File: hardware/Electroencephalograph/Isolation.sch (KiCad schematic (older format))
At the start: 14 parts, among them U4 THI3-0511, U5 ADUM2401BRWZ

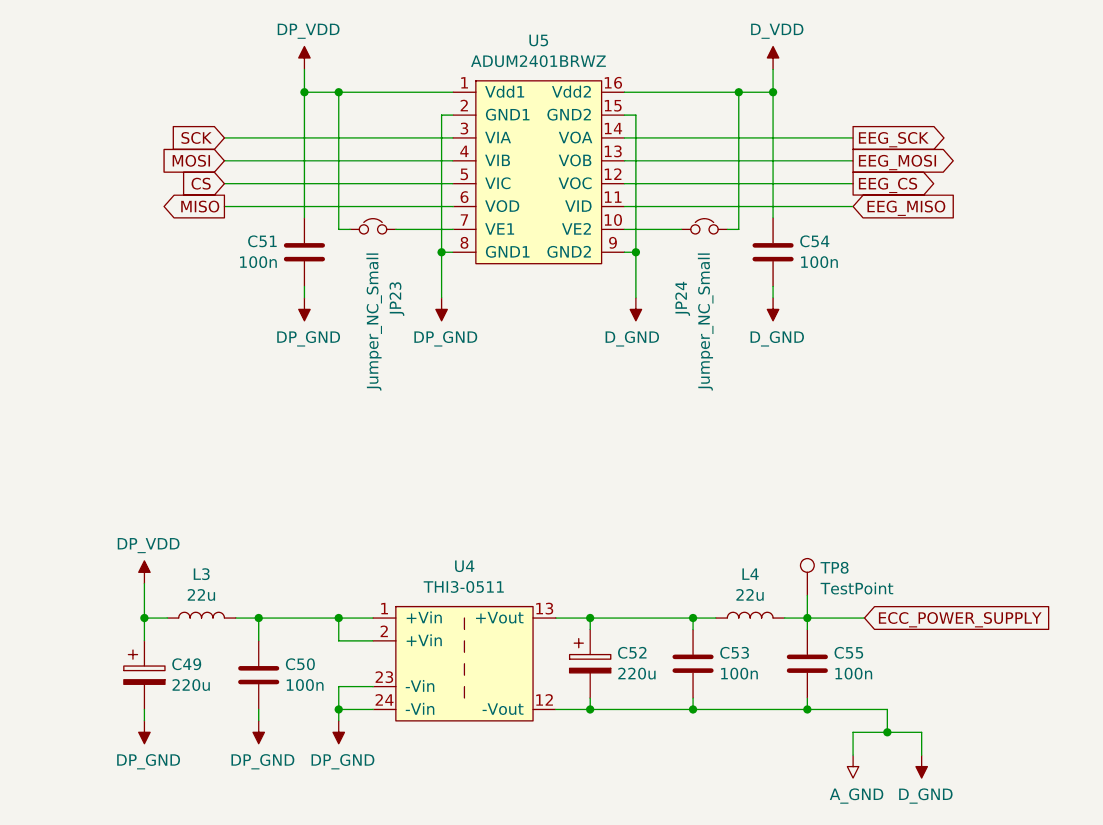
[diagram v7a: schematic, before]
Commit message: placing components groups
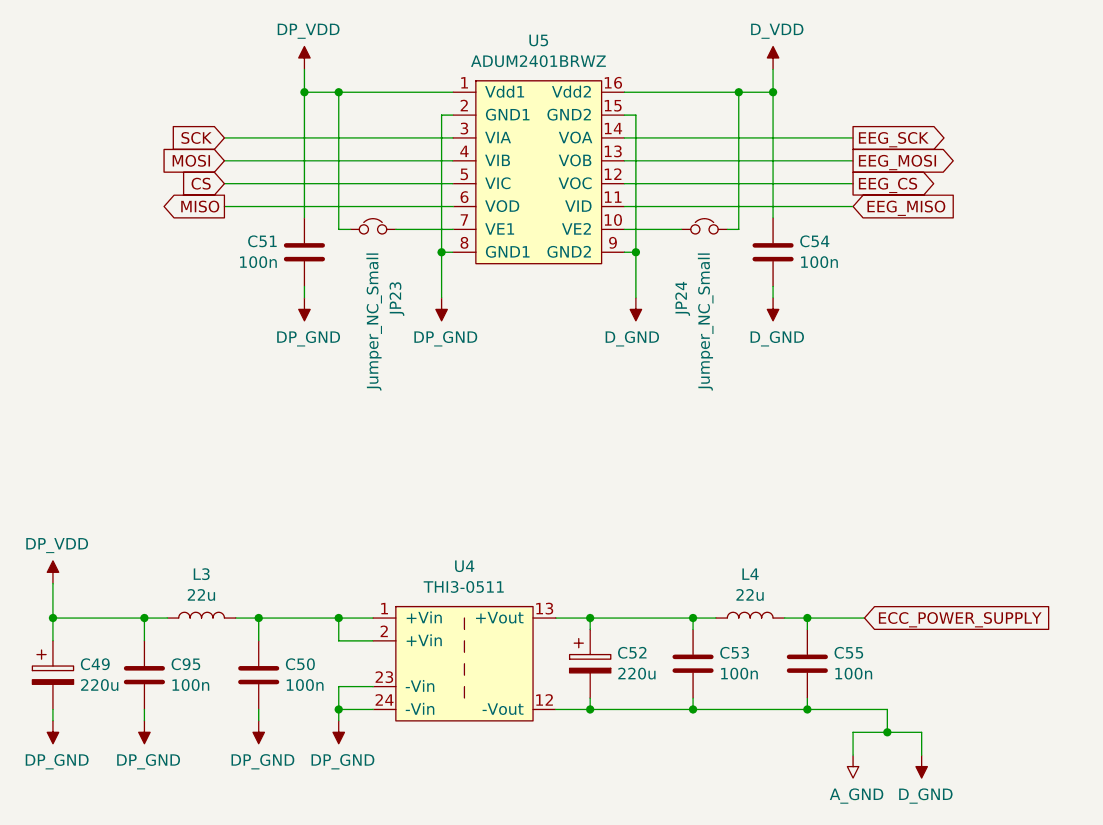
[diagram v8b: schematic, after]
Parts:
- removed TP8: TestPoint, TestPoint:TestPoint_Pad_1.5x1.5mm, symbol Connector:TestPoint
- added C95: 100n, Capacitor_SMD:C_0402_1005Metric, symbol Device:C
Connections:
- net GNDA: now also C95.2
- net VDDA: now also C95.1
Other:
- moved on the sheet: C49
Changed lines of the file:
@@
 $EndDescr
-$Comp
-L Electroencephalograph:ADUM2401BRWZ U5
-U 1 1 5E006D91
-P 3550 2350
-F 0 "U5" H 3525 2425 50  0000 C CNN
-F 1 "ADUM2401BRWZ" H 3525 2334 50  0000 C CNN
-F 2 "Package_SO:SOIC-16W_7.5x10.3mm_P1.27mm" H 3550 2350 50  0001 C CNN
-F 3 "" H 3550 2350 50  0001 C CNN
-	1    3550 2350
-	1    0    0    -1
-$EndComp
 $Comp
 L Electroencephalograph:D_GND #PWR?
@@
 	3150 3200 3100 3200
 Wire Wire Line
-	3100 3200 3100 3400
-Wire Wire Line
 	3150 2600 3100 2600
 Wire Wire Line
 	3100 2600 3100 3200
-Connection ~ 3100 3200
 Text GLabel 2150 2700 0    50   Input ~ 0
 SCK
@@
 Wire Wire Line
 	3150 3000 2150 3000
-Wire Wire Line
-	2500 3400 2500 3350
 Connection ~ 2500 2500
 Wire Wire Line
@@
 	2650 2500 2500 2500
 $Comp
-L Electroencephalograph:DP_GND #PWR104
-U 1 1 5E02E89B
-P 3100 3400
-F 0 "#PWR104" H 3100 3425 50  0001 C CNN
-F 1 "DP_GND" H 3117 3227 50  0000 C CNN
-F 2 "" H 3100 3425 50  0001 C CNN
-F 3 "" H 3100 3425 50  0001 C CNN
-	1    3100 3400
-	1    0    0    -1
-$EndComp
-$Comp
-L Electroencephalograph:DP_GND #PWR102
-U 1 1 5E02EFAB
-P 2500 3400
-F 0 "#PWR102" H 2500 3425 50  0001 C CNN
-F 1 "DP_GND" H 2517 3227 50  0000 C CNN
-F 2 "" H 2500 3425 50  0001 C CNN
-F 3 "" H 2500 3425 50  0001 C CNN
-	1    2500 3400
-	1    0    0    -1
-$EndComp
-$Comp
-L Electroencephalograph:THI3-0511 U4
-U 1 1 5E036623
-P 3200 4600
-F 0 "U4" H 3200 4625 50  0000 C CNN
-F 1 "THI3-0511" H 3200 4534 50  0000 C CNN
-F 2 "Electroencephalograph:THI3-0511" H 3200 4600 50  0001 C CNN
-F 3 "https://www.tme.eu/Document/dbc573554d903d2de79b1454bccf4b94/thi3-datasheet.pdf" H 3200 4600 50  0001 C CNN
-	1    3200 4600
-	1    0    0    -1
-$EndComp
-$Comp
 L Device:C C?
 U 1 1 5E036F39
@@
 	2650 5100 2650 5200
 Wire Wire Line
-	2300 5250 2300 5200
-Wire Wire Line
 	4900 5300 4900 5400
 Wire Wire Line
-	4900 5300 5050 5300
-Wire Wire Line
 	5200 5300 5200 5400
 Wire Wire Line
 	2800 5200 2650 5200
-Connection ~ 2650 5200
-Wire Wire Line
-	2650 5200 2650 5250
 Wire Wire Line
 	4700 4800 4700 4850
@@
 	5050 5200 5050 5300
 Connection ~ 4700 5200
-Connection ~ 5050 5300
-Wire Wire Line
-	5050 5300 5200 5300
 $Comp
 L Device:L L3
@@
 ECC_POWER_SUPPLY
 $Comp
-L Connector:TestPoint TP?
-U 1 1 5E1B3787
-P 4700 4700
-AR Path="/5DF61103/5E1B3787" Ref="TP?"  Part="1"
-AR Path="/5DFE0AD6/5E1B3787" Ref="TP8"  Part="1"
-F 0 "TP8" H 4758 4818 50  0000 L CNN
-F 1 "TestPoint" H 4758 4727 50  0000 L CNN
-F 2 "TestPoint:TestPoint_Pad_1.5x1.5mm" H 4900 4700 50  0001 C CNN
-F 3 "~" H 4900 4700 50  0001 C CNN
-	1    4700 4700
-	1    0    0    -1
-$EndComp
-Wire Wire Line
-	4700 4700 4700 4800
-$Comp
-L Electroencephalograph:DP_GND #PWR103
-U 1 1 5E00C6AB
-P 2650 5250
-F 0 "#PWR103" H 2650 5275 50  0001 C CNN
-F 1 "DP_GND" H 2667 5077 50  0000 C CNN
-F 2 "" H 2650 5275 50  0001 C CNN
-F 3 "" H 2650 5275 50  0001 C CNN
-	1    2650 5250
-	1    0    0    -1
-$EndComp
-$Comp
-L Electroencephalograph:DP_GND #PWR100
-U 1 1 5E00CF9A
-P 2300 5250
-F 0 "#PWR100" H 2300 5275 50  0001 C CNN
-F 1 "DP_GND" H 2317 5077 50  0000 C CNN
-F 2 "" H 2300 5275 50  0001 C CNN
-F 3 "" H 2300 5275 50  0001 C CNN
-	1    2300 5250
-	1    0    0    -1
-$EndComp
-$Comp
 L Device:CP C49
 U 1 1 5E035319
-P 1800 5050
-F 0 "C49" H 1918 5096 50  0000 L CNN
-F 1 "220u" H 1918 5005 50  0000 L CNN
-F 2 "Capacitor_SMD:CP_Elec_6.3x5.8" H 1838 4900 50  0001 C CNN
-F 3 "~" H 1800 5050 50  0001 C CNN
-	1    1800 5050
+P 1400 5050
+F 0 "C49" H 1518 5096 50  0000 L CNN
+F 1 "220u" H 1518 5005 50  0000 L CNN
+F 2 "Capacitor_SMD:CP_Elec_6.3x5.8" H 1438 4900 50  0001 C CNN
+F 3 "~" H 1400 5050 50  0001 C CNN
+	1    1400 5050
 	1    0    0    -1
 $EndComp
@@
 L Electroencephalograph:DP_GND #PWR99
 U 1 1 5E03B877
-P 1800 5250
-F 0 "#PWR99" H 1800 5275 50  0001 C CNN
-F 1 "DP_GND" H 1817 5077 50  0000 C CNN
-F 2 "" H 1800 5275 50  0001 C CNN
-F 3 "" H 1800 5275 50  0001 C CNN
-	1    1800 5250
-	1    0    0    -1
-$EndComp
-Wire Wire Line
-	1800 5250 1800 5200
+P 1400 5250
+F 0 "#PWR99" H 1400 5275 50  0001 C CNN
+F 1 "DP_GND" H 1417 5077 50  0000 C CNN
+F 2 "" H 1400 5275 50  0001 C CNN
+F 3 "" H 1400 5275 50  0001 C CNN
+	1    1400 5250
+	1    0    0    -1
+$EndComp
+Wire Wire Line
+	1400 5250 1400 5200
 Wire Wire Line
 	2800 4800 2650 4800
@@
 	2300 4800 2300 4900
 Wire Wire Line
-	1800 4650 1800 4800
+	1400 4650 1400 4800
 Wire Wire Line
 	2300 4800 2200 4800
@@
 Wire Wire Line
 	1900 4800 1800 4800
-Connection ~ 1800 4800
-Wire Wire Line
-	1800 4800 1800 4900
+Connection ~ 1400 4800
+Wire Wire Line
+	1400 4800 1400 4900
 $Comp
 L Device:CP C52
@@
 L Electroencephalograph:DP_VDD #PWR98
 U 1 1 5E00C2CC
-P 1800 4650
-F 0 "#PWR98" H 1800 4775 50  0001 C CNN
-F 1 "DP_VDD" H 1817 4823 50  0000 C CNN
-F 2 "" H 1800 4775 50  0001 C CNN
-F 3 "" H 1800 4775 50  0001 C CNN
-	1    1800 4650
+P 1400 4650
+F 0 "#PWR98" H 1400 4775 50  0001 C CNN
+F 1 "DP_VDD" H 1417 4823 50  0000 C CNN
+F 2 "" H 1400 4775 50  0001 C CNN
+F 3 "" H 1400 4775 50  0001 C CNN
+	1    1400 4650
 	1    0    0    -1
 $EndComp
@@
 	1    0    0    -1
 $EndComp
+$Comp
+L Device:C C?
+U 1 1 5E1125B2
+P 1800 5050
+AR Path="/5DF4CFF8/5E1125B2" Ref="C?"  Part="1"
+AR Path="/5DF61103/5E1125B2" Ref="C?"  Part="1"
+AR Path="/5DFE0AD6/5E1125B2" Ref="C95"  Part="1"
+F 0 "C95" H 1915 5096 50  0000 L CNN
+F 1 "100n" H 1915 5005 50  0000 L CNN
+F 2 "Capacitor_SMD:C_0402_1005Metric" H 1838 4900 50  0001 C CNN
+F 3 "~" H 1800 5050 50  0001 C CNN
+	1    1800 5050
+	1    0    0    -1
+$EndComp
+Wire Wire Line
+	1800 4900 1800 4800
+Connection ~ 1800 4800
+Wire Wire Line
+	1800 4800 1400 4800
+Wire Wire Line
+	4900 5300 5050 5300
+Connection ~ 5050 5300
+Wire Wire Line
+	5050 5300 5200 5300
+$Comp
+L Electroencephalograph:DP_GND #PWR177
+U 1 1 5E1125B9
+P 1800 5250
+F 0 "#PWR177" H 1800 5275 50  0001 C CNN
+F 1 "DP_GND" H 1817 5077 50  0000 C CNN
+F 2 "" H 1800 5275 50  0001 C CNN
+F 3 "" H 1800 5275 50  0001 C CNN
+	1    1800 5250
+	1    0    0    -1
+$EndComp
+Wire Wire Line
+	1800 5250 1800 5200
+$Comp
+L Electroencephalograph:DP_GND #PWR100
+U 1 1 5E00CF9A
+P 2300 5250
+F 0 "#PWR100" H 2300 5275 50  0001 C CNN
+F 1 "DP_GND" H 2317 5077 50  0000 C CNN
+F 2 "" H 2300 5275 50  0001 C CNN
+F 3 "" H 2300 5275 50  0001 C CNN
+	1    2300 5250
+	1    0    0    -1
+$EndComp
+$Comp
+L Electroencephalograph:DP_GND #PWR103
+U 1 1 5E00C6AB
+P 2650 5250
+F 0 "#PWR103" H 2650 5275 50  0001 C CNN
+F 1 "DP_GND" H 2667 5077 50  0000 C CNN
+F 2 "" H 2650 5275 50  0001 C CNN
+F 3 "" H 2650 5275 50  0001 C CNN
+	1    2650 5250
+	1    0    0    -1
+$EndComp
+Connection ~ 2650 5200
+Wire Wire Line
+	2650 5200 2650 5250
+Wire Wire Line
+	2300 5250 2300 5200
+$Comp
+L Electroencephalograph:DP_GND #PWR102
+U 1 1 5E02EFAB
+P 2500 3400
+F 0 "#PWR102" H 2500 3425 50  0001 C CNN
+F 1 "DP_GND" H 2517 3227 50  0000 C CNN
+F 2 "" H 2500 3425 50  0001 C CNN
+F 3 "" H 2500 3425 50  0001 C CNN
+	1    2500 3400
+	1    0    0    -1
+$EndComp
+$Comp
+L Electroencephalograph:DP_GND #PWR104
+U 1 1 5E02E89B
+P 3100 3400
+F 0 "#PWR104" H 3100 3425 50  0001 C CNN
+F 1 "DP_GND" H 3117 3227 50  0000 C CNN
+F 2 "" H 3100 3425 50  0001 C CNN
+F 3 "" H 3100 3425 50  0001 C CNN
+	1    3100 3400
+	1    0    0    -1
+$EndComp
+Wire Wire Line
+	2500 3400 2500 3350
+Connection ~ 3100 3200
+Wire Wire Line
+	3100 3200 3100 3400
+$Comp
+L Electroencephalograph:ADUM2401BRWZ U5
+U 1 1 5E006D91
+P 3550 2350
+F 0 "U5" H 3525 2425 50  0000 C CNN
+F 1 "ADUM2401BRWZ" H 3525 2334 50  0000 C CNN
+F 2 "Package_SO:SOIC-16W_7.5x10.3mm_P1.27mm" H 3550 2350 50  0001 C CNN
+F 3 "" H 3550 2350 50  0001 C CNN
+	1    3550 2350
+	1    0    0    -1
+$EndComp
+$Comp
+L Electroencephalograph:THI3-0511 U4
+U 1 1 5E036623
+P 3200 4600
+F 0 "U4" H 3200 4625 50  0000 C CNN
+F 1 "THI3-0511" H 3200 4534 50  0000 C CNN
+F 2 "Electroencephalograph:THI3-0511" H 3200 4600 50  0001 C CNN
+F 3 "https://www.tme.eu/Document/dbc573554d903d2de79b1454bccf4b94/thi3-datasheet.pdf" H 3200 4600 50  0001 C CNN
+	1    3200 4600
+	1    0    0    -1
+$EndComp
